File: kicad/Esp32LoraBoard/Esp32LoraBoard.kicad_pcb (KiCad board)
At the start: 2 copper layers, 71.8 x 64.1 mm, 49 parts, among them J1 USB_B_Micro, J2 Power-Selector, J3 Testpoints, J4 ESP_PROG_JTAG, J5 Prog, J6 ext_Measure, J7 Measurement-Selector, J8 OLED_128x64, Q1 UMH3N, Q2 Si2302DS_NMOS, Q3 Si2301DS_PMOS, Q4 Si2302DS_NMOS, Q5 Si2301DS_PMOS, Q6 Si2302DS_NMOS, SW1 Rotary_Encoder, U1 LM3940IMP-3.3, U2 ESP32-WROOM-32, U3 RFM95W-868S2

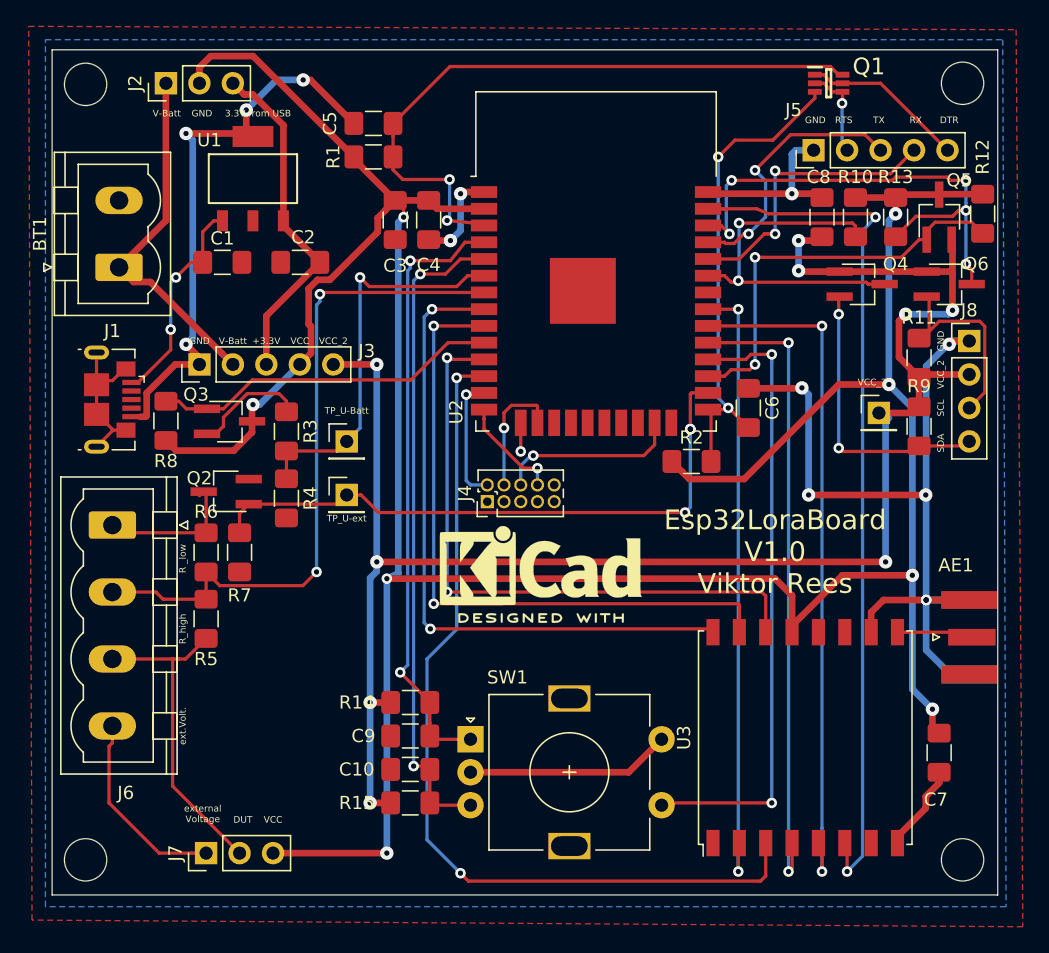
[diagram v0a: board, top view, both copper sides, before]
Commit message: Reset Button added
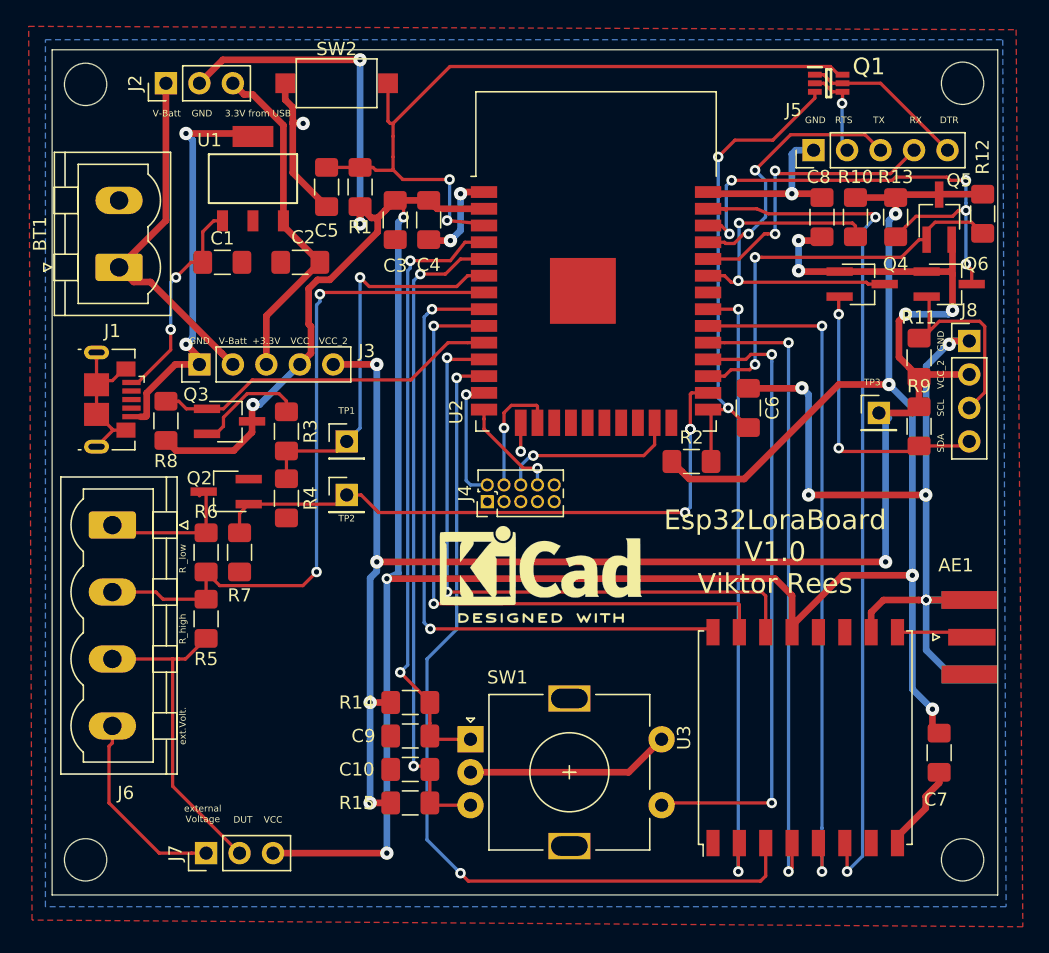
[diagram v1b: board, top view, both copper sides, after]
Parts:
- added SW2: Reset, Button_Switch_SMD:SW_SPST_CK_RS282G05A3, F.Cu at (125.7, 61.0)
- moved C5 5.99 mm to (125.0, 68.8), turned to 270 degrees
- moved R1 2.50 mm to (127.5, 68.8), turned to 90 degrees
- renumbered TP_U-Batt to TP1, TP_U-ext to TP2, VCC_2 to TP3
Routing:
- net /Reset: track 50.4 -> 58.9 mm
- net VCC: track 235.7 -> 243.1 mm, vias 8 -> 10
- net GND: track 153.9 -> 152.7 mm, vias 14 -> 13

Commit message: Reset Circuit modified. C5 = 100nF now in order to enter programming mode after reset
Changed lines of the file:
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@@
     (tags "resistor handsolder")
     (attr smd)
-    (fp_text reference R2 (at 0 -1.82) (layer F.SilkS)
+    (fp_text reference R2 (at -3.556 0.127) (layer F.SilkS)
       (effects (font (size 1 1) (thickness 0.15)))
     )
@@
     (tags "resistor handsolder")
     (attr smd)
-    (fp_text reference R9 (at -3.048 0) (layer F.SilkS)
-      (effects (font (size 1 1) (thickness 0.15)))
-    )
+    (fp_text reference R9 (at 3.175 0) (layer F.SilkS)
+      (effects (font (size 1 1) (thickness 0.15)))
+    )

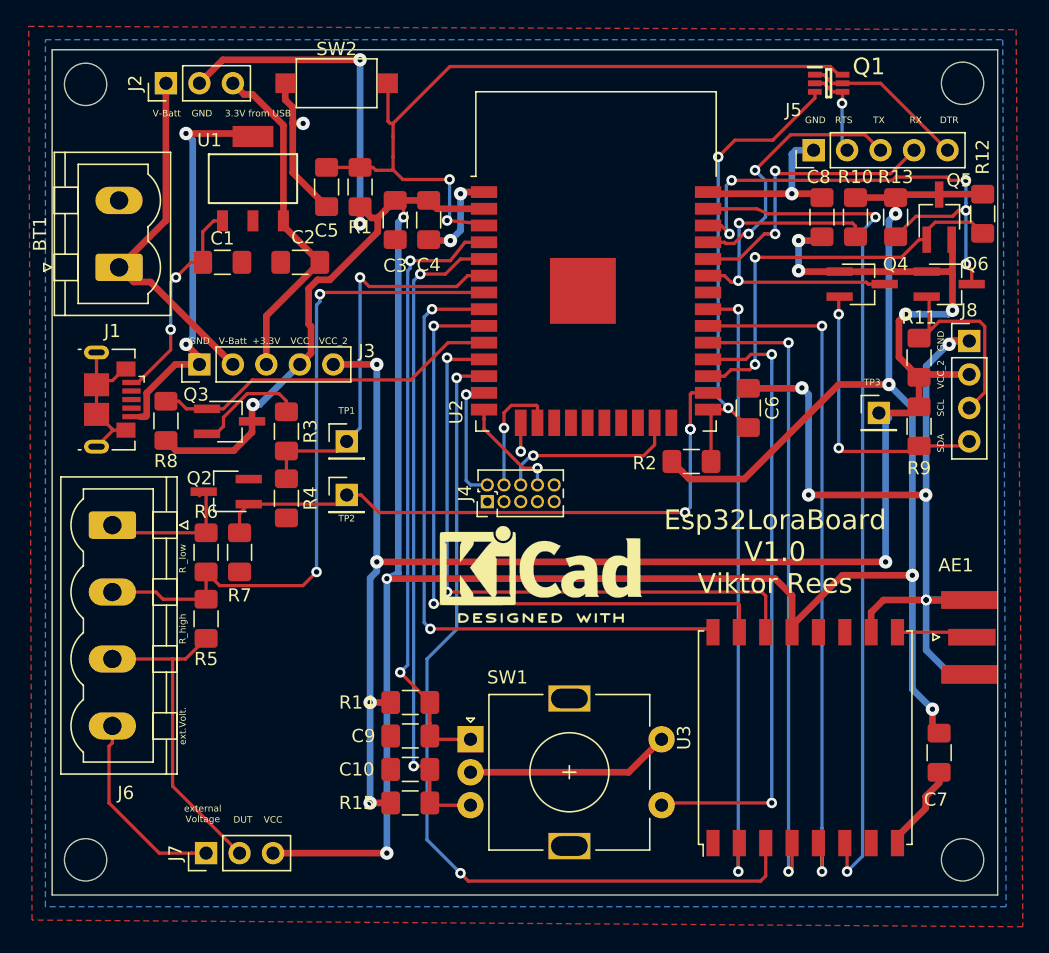
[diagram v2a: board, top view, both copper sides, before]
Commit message: exchanged RX/TX and Boot/Reset wires
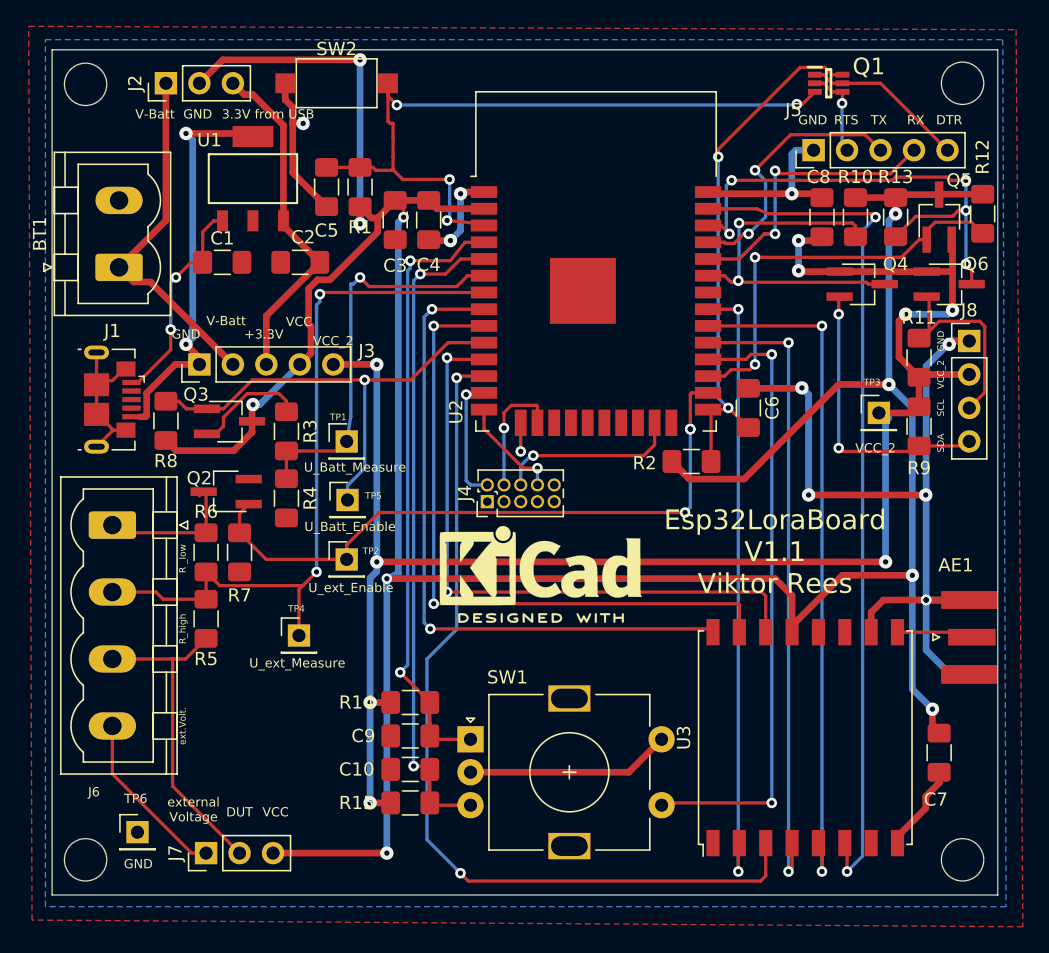
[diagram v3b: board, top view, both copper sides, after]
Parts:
- added TP4: U_EXT_MEASURE, Connector_PinHeader_2.54mm:PinHeader_1x01_P2.54mm_Vertical, F.Cu at (122.9, 102.9)
- added TP5: U_BAT_ENABLE, Connector_PinHeader_2.54mm:PinHeader_1x01_P2.54mm_Vertical, F.Cu at (126.6, 92.6)
- added TP6: GND, Connector_PinHeader_2.54mm:PinHeader_1x01_P2.54mm_Vertical, F.Cu at (110.6, 117.8)
- C5: value 1n -> 220n
- TP1: value TP_U_BATT -> U_BATT_MEASURE
- TP2: value TP_U_EXT -> U_EXT_ENABLE
- moved TP2 4.89 mm to (126.5, 97.1)
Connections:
- Q1 pad 3: /Boot -> /Reset
- Q1 pad 6: /Reset -> /Boot
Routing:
- net /UBAT_ENABLE: track 26.5 -> 36.1 mm, vias 0 -> 1
- net /U_EXT_MEASURE: track 52.3 -> 56.3 mm
- net /U_EXT_ENABLE: track 46.9 -> 50.1 mm
- net /Boot: track 36.7 -> 39.8 mm
- net /Reset: track 58.9 -> 56.8 mm, vias 2 -> 4
- net /ext.Voltage: track 14.9 -> 13.2 mm
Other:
- board text added: "Esp32LoraBoard V1.1 Viktor Rees"
- board text added: "U_Batt_Enable"
- board text added: "U_Batt_Measure"
- board text added: "U_ext_Enable"
- board text added: "U_ext_Measure"
- board text removed: "Esp32LoraBoard V1.0 Viktor Rees"
